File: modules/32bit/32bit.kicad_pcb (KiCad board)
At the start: 4 copper layers, 30.5 x 68.6 mm, 51 parts, among them J5 USB_C_Receptacle_USB2.0_14P, SW1 K2-1808SN-A4SW-01, SW2 K2-1808SN-A4SW-01, SW4 K2-1808SN-A4SW-01, U1 ESP32-S3-WROOM-1U-N16R8, U3 MCP6002-xSN

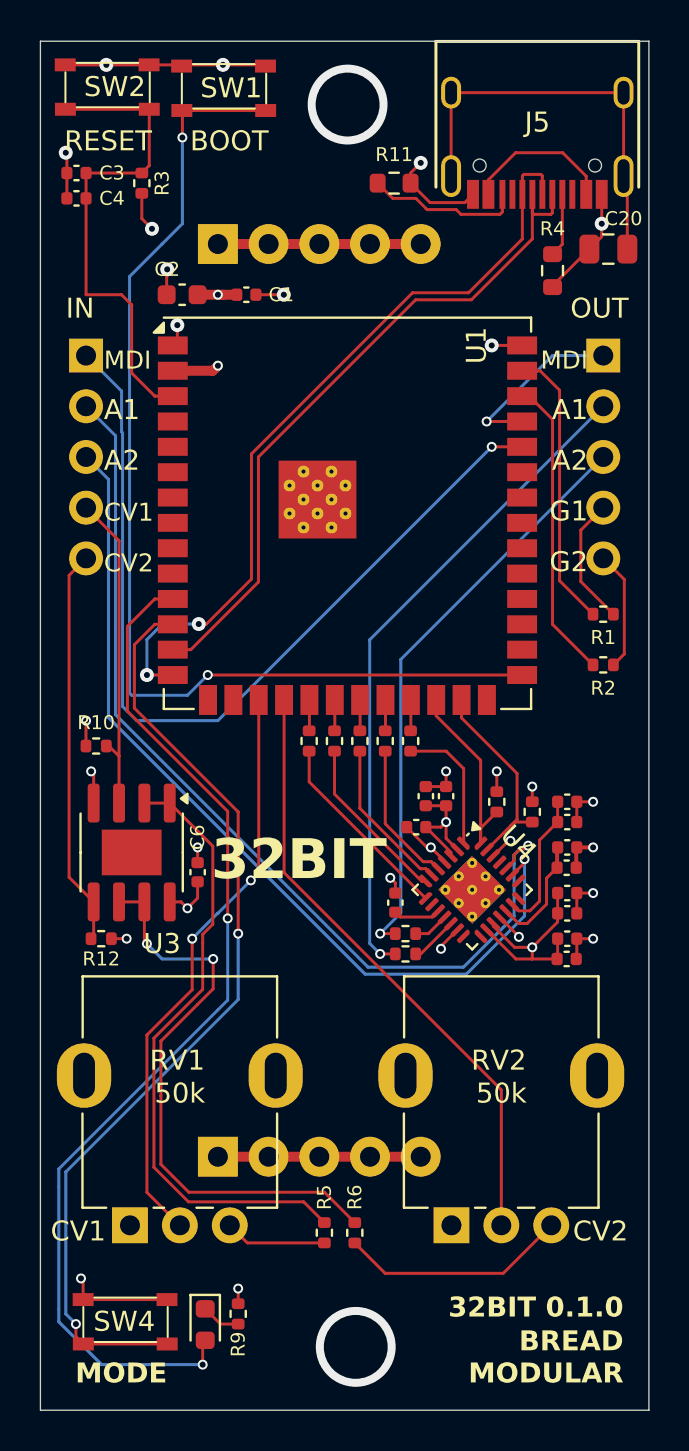
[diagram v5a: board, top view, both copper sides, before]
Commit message: Add a 3.3v island for es8388
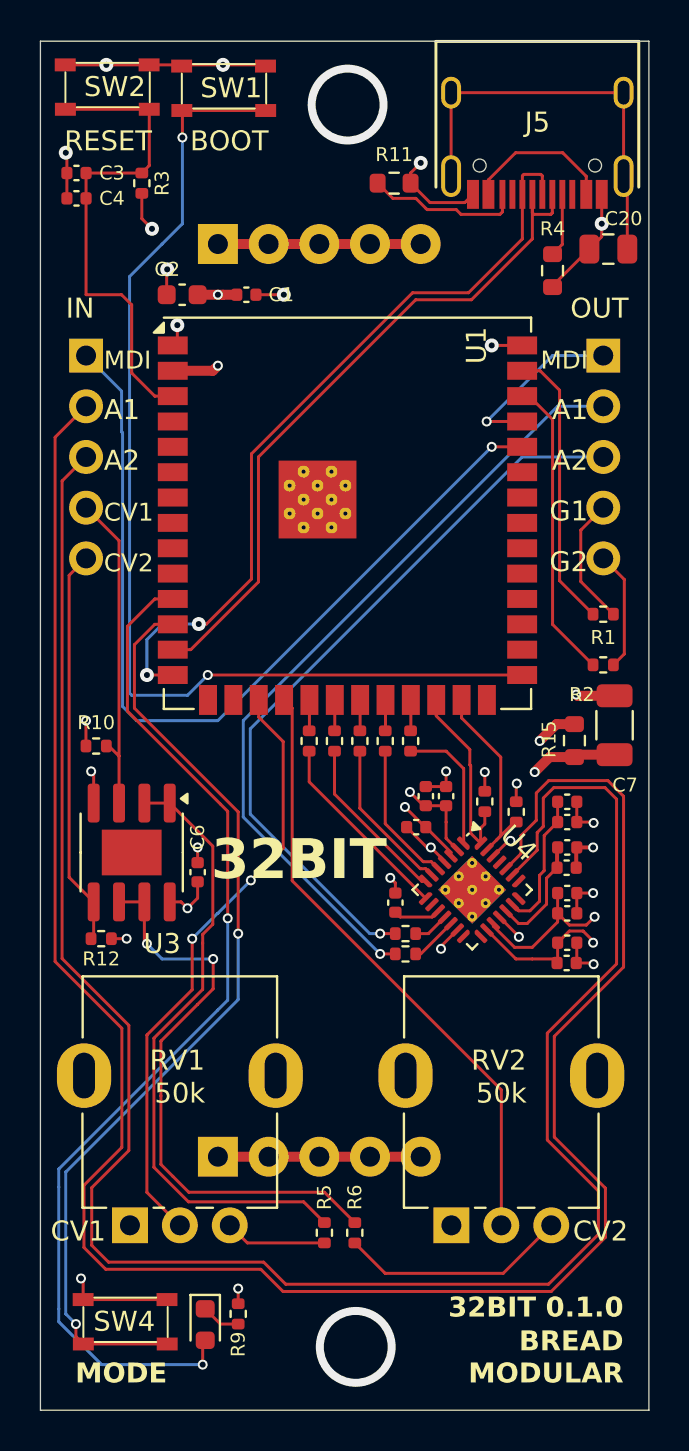
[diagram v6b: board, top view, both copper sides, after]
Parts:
- added C7: 100uf, Capacitor_SMD:C_1206_3216Metric, F.Cu at (75.8, 74.9)
- added R15: 10, Resistor_SMD:R_0603_1608Metric, F.Cu at (73.7, 75.7)
- moved R24 0.80 mm to (70.8, 79.2)
- moved R25 0.60 mm to (69.2, 78.7)
- moved C38 0.20 mm to (73.3, 86.8)
- moved C39 0.20 mm to (73.4, 85.8)
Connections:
- C21 pad 1: +3V3 -> +3V3_8388
- C22 pad 1: +3V3 -> +3V3_8388
- C26 pad 1: +3V3 -> +3V3_8388
- C37 pad 1: +3V3 -> +3V3_8388
- C38 pad 1: +3V3 -> +3V3_8388
- C39 pad 1: +3V3 -> +3V3_8388
- C5 pad 1: +3V3 -> +3V3_8388
- R24 pad 2: +3V3 -> +3V3_8388
- R25 pad 2: +3V3 -> +3V3_8388
- U4 pad 16: +3V3 -> +3V3_8388
- U4 pad 17: +3V3 -> +3V3_8388
- U4 pad 2: +3V3 -> +3V3_8388
- U4 pad 3: +3V3 -> +3V3_8388
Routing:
- net AIN_1: track 48.1 -> 107.1 mm, vias 1 -> 0
- net AIN_2: track 44.8 -> 102.3 mm, vias 1 -> 0
- net +3V3: track 135.2 -> 94.8 mm, vias 10 -> 7
- net +3V3_8388: track 0.00 -> 29.7 mm, vias 0 -> 7
- net AOUT_2: track 29.3 -> 37.3 mm
- net AOUT_1: track 33.3 -> 39.8 mm
- net GND: track 63.4 -> 65.7 mm, vias 23 -> 24
- net BUFF_CV1: track 29.3 -> 30.3 mm
- added copper zone on In2.Cu, net +3V3_8388

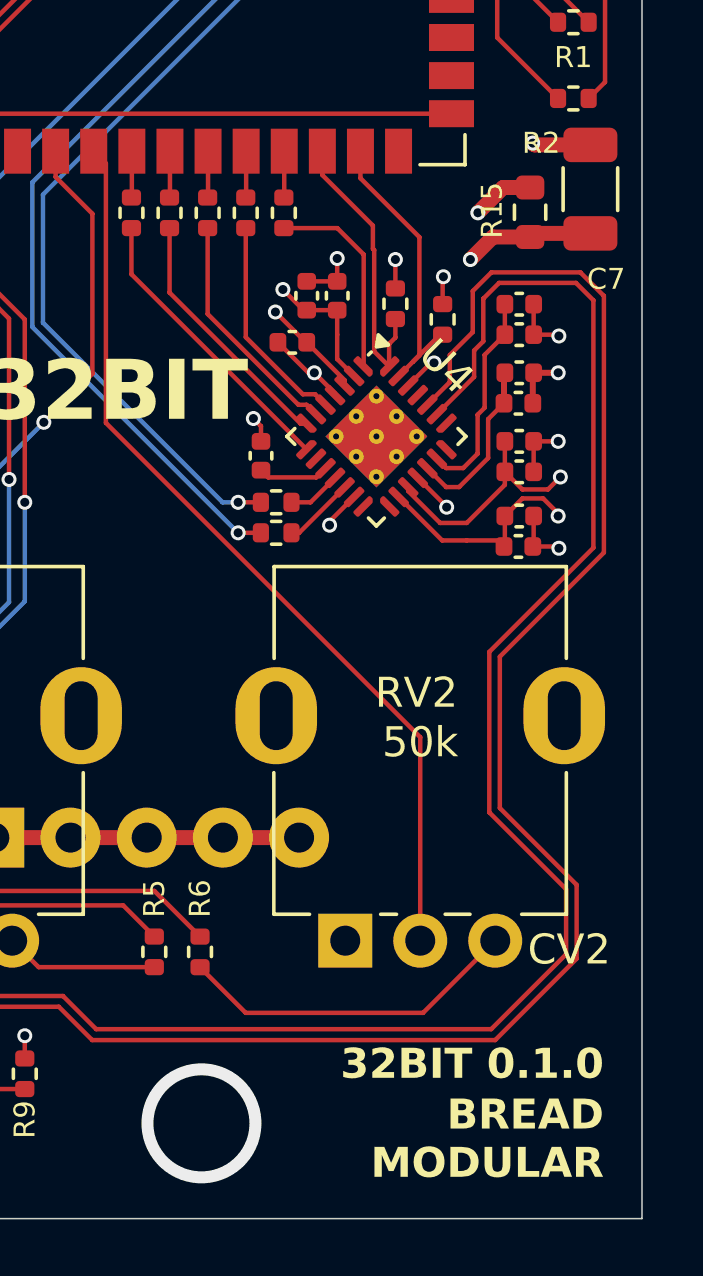
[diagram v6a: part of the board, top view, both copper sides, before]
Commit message: Add better routing for power
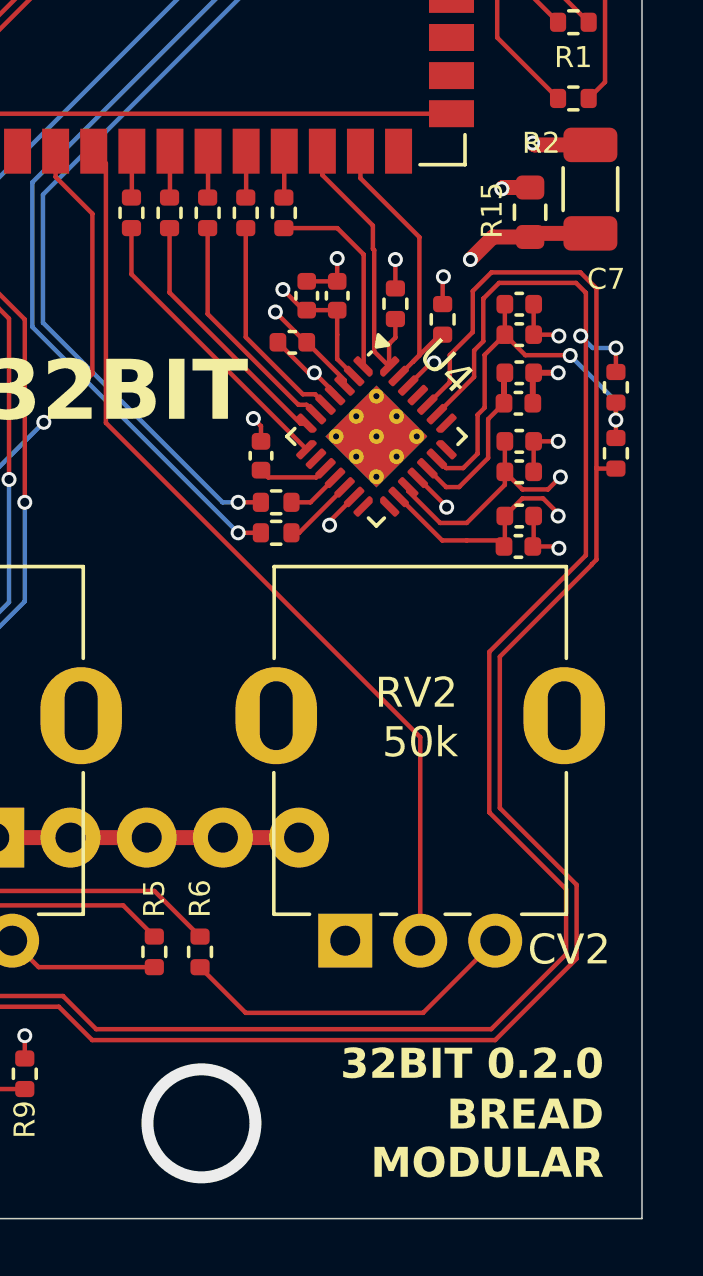
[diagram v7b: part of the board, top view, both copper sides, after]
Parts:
- added R16: 100k, Resistor_SMD:R_0402_1005Metric, F.Cu at (76.6, 81.5)
- added R19: 100k, Resistor_SMD:R_0402_1005Metric, F.Cu at (76.6, 83.7)
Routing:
- net Net-(U4-VMID): track 7.05 -> 13.5 mm, vias 0 -> 2
- net AIN_2: track 102.3 -> 104.2 mm, vias 0 -> 2
- net +3V3: track 94.8 -> 96.7 mm
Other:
- board text added: "32BIT 0.2.0"
- board text removed: "32BIT 0.1.0"

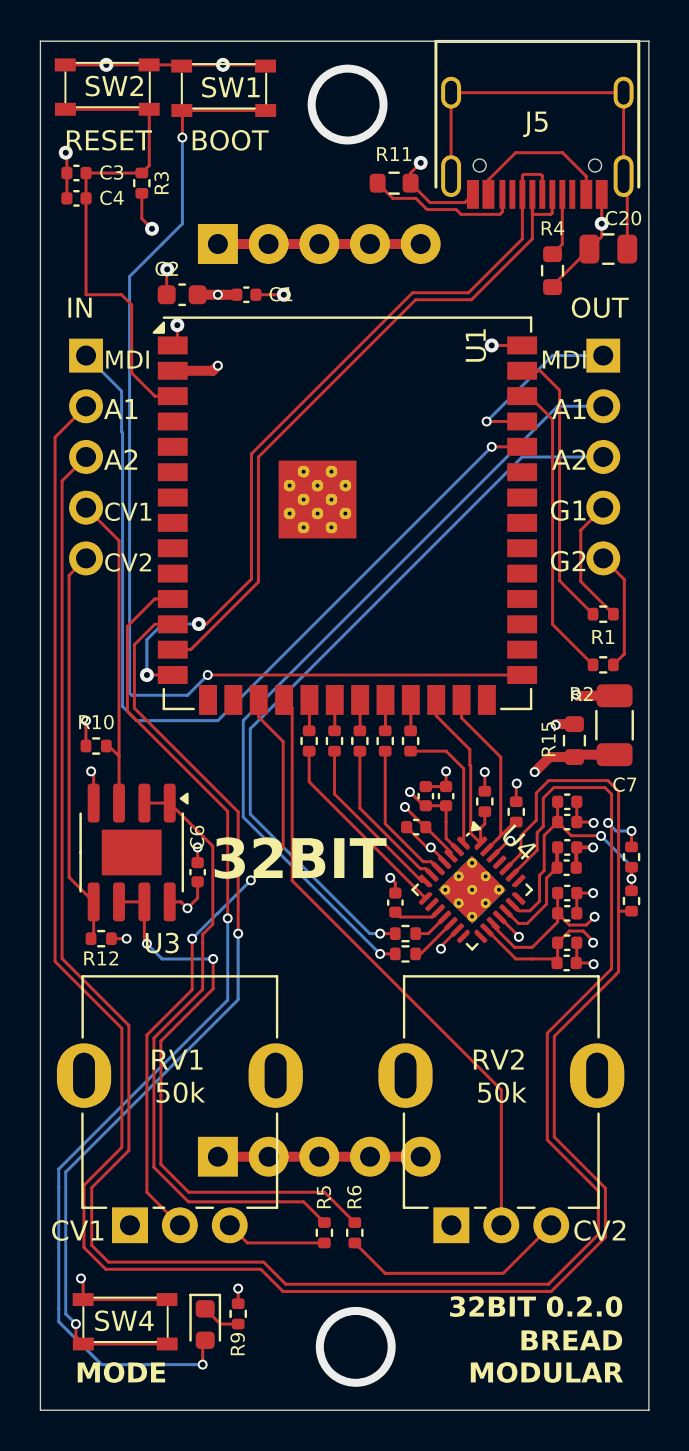
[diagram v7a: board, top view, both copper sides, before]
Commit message: Improve 32bit power supply
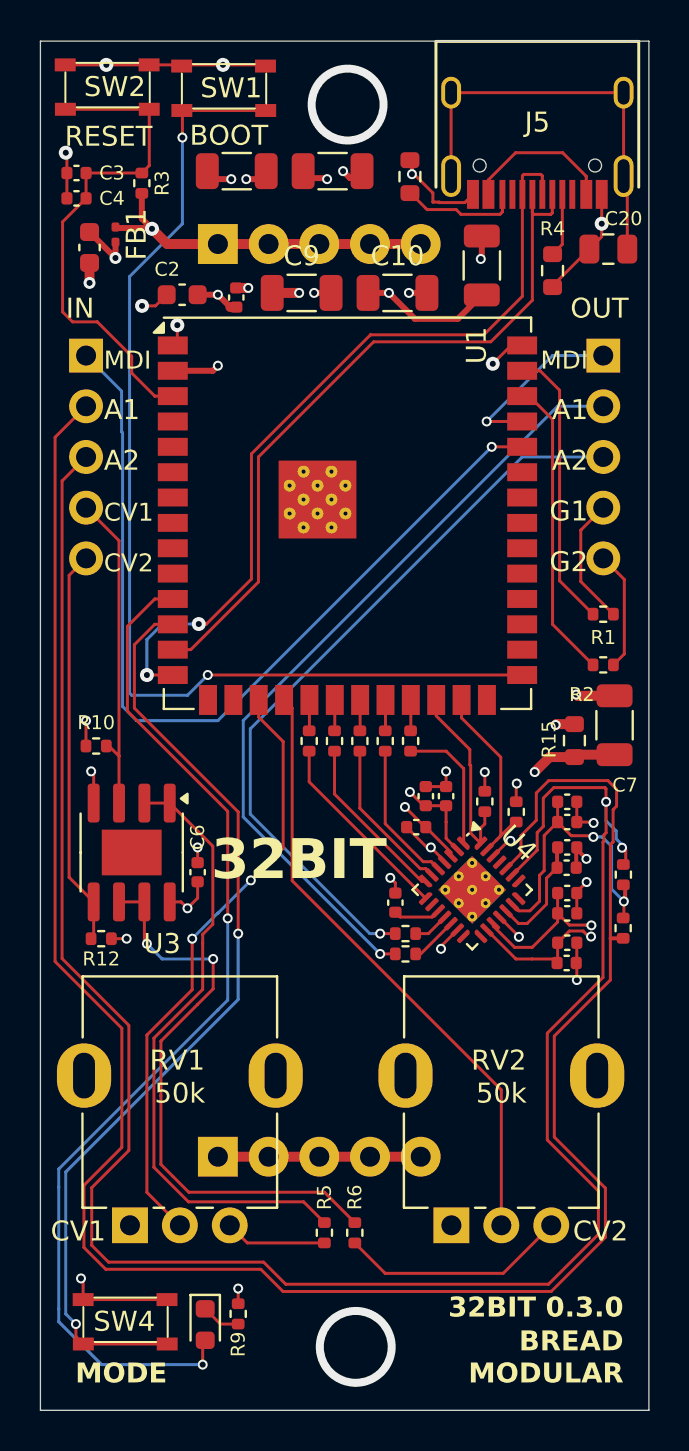
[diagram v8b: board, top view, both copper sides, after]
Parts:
- added C10: 100uf, Capacitor_SMD:C_1206_3216Metric, F.Cu at (64.9, 53.2)
- added C11: 100uf, Capacitor_SMD:C_1206_3216Metric, F.Cu at (56.8, 47.1)
- added C12: 100uf, Capacitor_SMD:C_1206_3216Metric, F.Cu at (61.6, 47.1)
- added C13: 100uf, Capacitor_SMD:C_1206_3216Metric, F.Cu at (69.1, 51.9)
- added C8: 10uf, Capacitor_SMD:C_0603_1608Metric, F.Cu at (49.5, 51.0)
- added C9: 100uf, Capacitor_SMD:C_1206_3216Metric, F.Cu at (60.1, 53.2)
- added FB1: BLM18PG121, Capacitor_SMD:C_0201_0603Metric, F.Cu at (50.8, 50.3)
- C2: value 22uf -> 10uf
- moved R19 1.42 mm to (76.2, 85.1)
- moved R16 0.97 mm to (76.2, 82.4)
- moved R11 0.86 mm to (65.5, 47.4), turned to 90 degrees
- moved C1 0.52 mm to (56.8, 53.5), turned to 90 degrees
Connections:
- C1 pad 1: +3V3 -> +3V3_ESP32
- C2 pad 1: +3V3 -> +3V3_ESP32
- U1 pad 2: +3V3 -> +3V3_ESP32
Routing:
- net +3V3_ESP32: track 0.00 -> 65.1 mm, vias 0 -> 7
- net +3V3: track 96.7 -> 89.6 mm, vias 7 -> 5
- net GND: track 65.7 -> 71.3 mm, vias 24 -> 31
- net Net-(J5-CC2): track 7.83 -> 5.59 mm
- net USB_D-: track 35.3 -> 37.1 mm
- net USB_D+: track 39.0 -> 40.7 mm
- net Net-(U4-VMID): track 13.5 -> 15.1 mm
- net AIN_2: track 104.2 -> 105.5 mm
- net Net-(SW2-B): track 24.9 -> 25.5 mm
- net +3V3_8388: track 29.7 -> 29.1 mm
- net (no net): vias 2 -> 1
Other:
- board text added: "32BIT 0.3.0"
- board text removed: "32BIT 0.2.0"
